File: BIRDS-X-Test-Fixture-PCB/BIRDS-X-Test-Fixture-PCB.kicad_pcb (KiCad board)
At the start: 2 copper layers, 0 parts

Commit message: Layout and label PCB
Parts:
- added C101: 100n, Capacitor_SMD:C_1206_3216Metric_Pad1.33x1.80mm_HandSolder, F.Cu at (91.7, 43.3)
- added D_3V3: LED, LED_SMD:LED_1206_3216Metric_Pad1.42x1.75mm_HandSolder, F.Cu at (117.1, 90.1)
- added D_5V0: LED, LED_SMD:LED_1206_3216Metric_Pad1.42x1.75mm_HandSolder, F.Cu at (117.1, 73.6)
- added H1: MountingHole, MountingHole:MountingHole_4mm, F.Cu at (81.5, 43.3)
- added H2: MountingHole, MountingHole:MountingHole_4mm, F.Cu at (81.5, 132.2)
- added H3: MountingHole, MountingHole:MountingHole_4mm, F.Cu at (169.2, 132.2)
- added H4: MountingHole, MountingHole:MountingHole_4mm, F.Cu at (169.2, 43.3)
- added H_3V3_1: MountingHole_Pad, MountingHole:MountingHole_4mm_Pad_Via, F.Cu at (125.6, 132.2)
- added H_3V3_2: MountingHole_Pad, MountingHole:MountingHole_4mm_Pad_Via, F.Cu at (135.7, 132.2)
- added H_5V_1: MountingHole_Pad, MountingHole:MountingHole_4mm_Pad_Via, F.Cu at (147.2, 132.2)
- added H_5V_2: MountingHole_Pad, MountingHole:MountingHole_4mm_Pad_Via, F.Cu at (156.5, 132.2)
- added H_GND_1: MountingHole_Pad, MountingHole:MountingHole_4mm_Pad_Via, F.Cu at (114.1, 132.2)
- added H_GND_2: MountingHole_Pad, MountingHole:MountingHole_4mm_Pad_Via, F.Cu at (104.4, 132.2)
- added H_GND_3: MountingHole_Pad, MountingHole:MountingHole_4mm_Pad_Via, F.Cu at (94.6, 132.2)
- added J101: LPC-50M2LG, Connector_PinHeader_2.00mm:PinHeader_2x25_P2.00mm_Horizontal, F.Cu at (81.0, 112.3)
- added J102: Conn_01x05, Connector_PinHeader_2.54mm:PinHeader_1x05_P2.54mm_Vertical, F.Cu at (148.6, 82.5)
- added J103: ~, Connector_PinHeader_2.54mm:PinHeader_2x25_P2.54mm_Vertical, F.Cu at (129.8, 119.5)
- added J104: ~, Connector_PinHeader_2.54mm:PinHeader_2x25_P2.54mm_Vertical, F.Cu at (96.8, 119.5)
- added J105: Conn_01x06, Connector_PinHeader_2.54mm:PinHeader_1x06_P2.54mm_Vertical, F.Cu at (105.7, 58.5)
- added J109: Conn_01x05, Connector_PinHeader_2.54mm:PinHeader_1x05_P2.54mm_Vertical, F.Cu at (166.6, 52.2)
- added J110: Conn_02x05_Odd_Even, Connector_IDC:IDC-Header_2x05_P2.54mm_Latch_Vertical, F.Cu at (166.6, 77.6)
- added J111: Conn_02x05_Odd_Even, Connector_IDC:IDC-Header_2x05_P2.54mm_Latch_Vertical, F.Cu at (150.1, 52.2)
- added JP101: Jumper_3_Open, Connector_PinHeader_2.54mm:PinHeader_1x03_P2.54mm_Vertical, F.Cu at (113.0, 59.7)
- added J_3V3_1: Screw_Terminal_01x02, TerminalBlock:TerminalBlock_bornier-2_P5.08mm, F.Cu at (132.3, 43.3)
- added J_3V3_2: Screw_Terminal_01x02, TerminalBlock:TerminalBlock_bornier-2_P5.08mm, F.Cu at (167.9, 109.3)
- added J_5V_1: Screw_Terminal_01x02, TerminalBlock:TerminalBlock_bornier-2_P5.08mm, F.Cu at (167.9, 120.8)
- added J_5V_2: Screw_Terminal_01x02, TerminalBlock:TerminalBlock_bornier-2_P5.08mm, F.Cu at (119.6, 43.3)
- added R_3V3: 1k, Resistor_THT:R_Axial_DIN0411_L9.9mm_D3.6mm_P12.70mm_Horizontal, F.Cu at (112.0, 83.9)
- added R_5V0: 2.2k, Resistor_THT:R_Axial_DIN0411_L9.9mm_D3.6mm_P12.70mm_Horizontal, F.Cu at (112.0, 66.2)
- added SW_3V3_EN_DIO1: SW_SPDT, Button_Switch_THT:SW_Slide_1P2T_CK_OS102011MS2Q, F.Cu at (101.7, 50.4)
- added SW_5V_EN_DIO2: SW_SPDT, Button_Switch_THT:SW_Slide_1P2T_CK_OS102011MS2Q, F.Cu at (108.2, 50.4)
- added SW_RST1: SW_Push, Button_Switch_THT:SW_PUSH_6mm, F.Cu at (88.2, 48.5)
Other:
- board outline added: 97.3 x 99.3 mm
- board text added: "3V"
- board text added: "3V3 EN"
- board text added: "5V"
- board text added: "5V EN"
- board text added: "DIO Level"
- board text added: "G"
- board text added: "RX"
- board text added: "ST_CLK"
- board text added: "ST_DIO"
- board text added: "ST_RST"
- board text added: "SW: Triangle =+V=ON"
- board text added: "TX"
- board text added: "TX,RX"

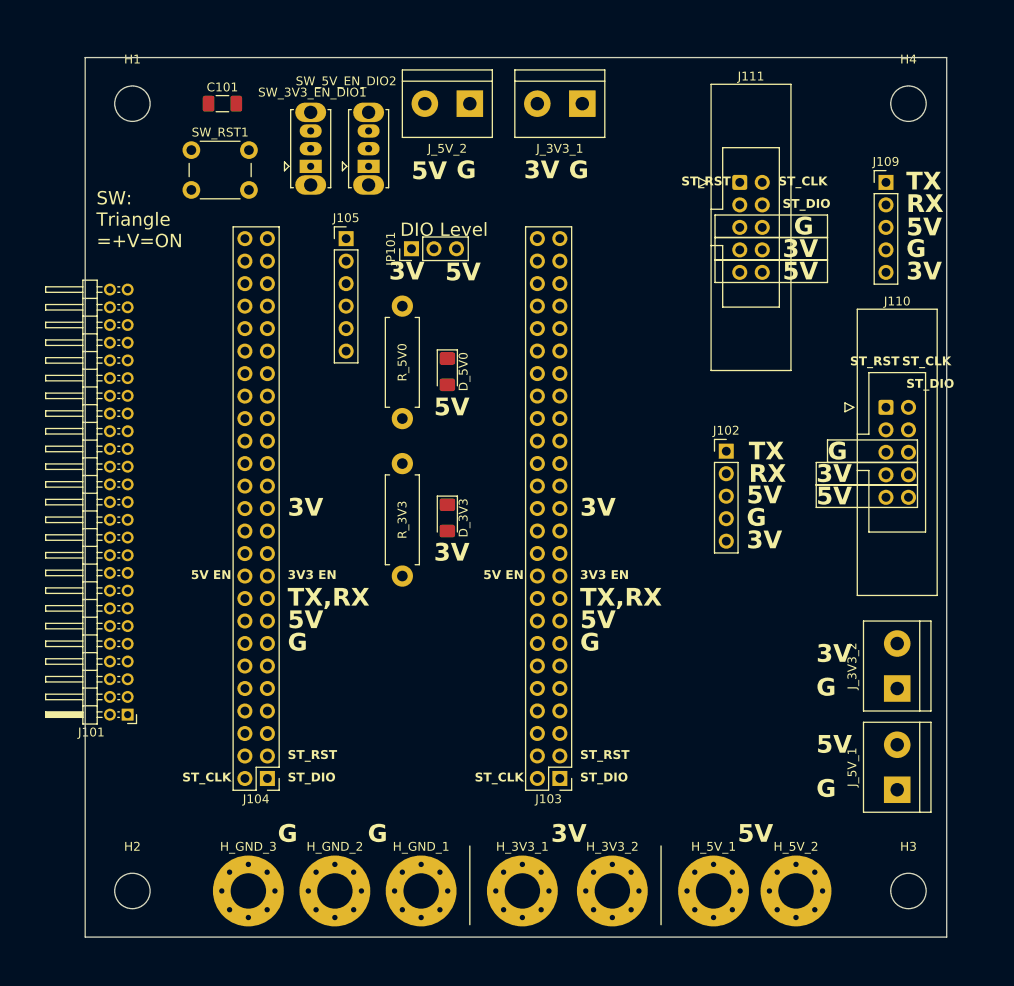
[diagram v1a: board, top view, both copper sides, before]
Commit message: Finish test fixture
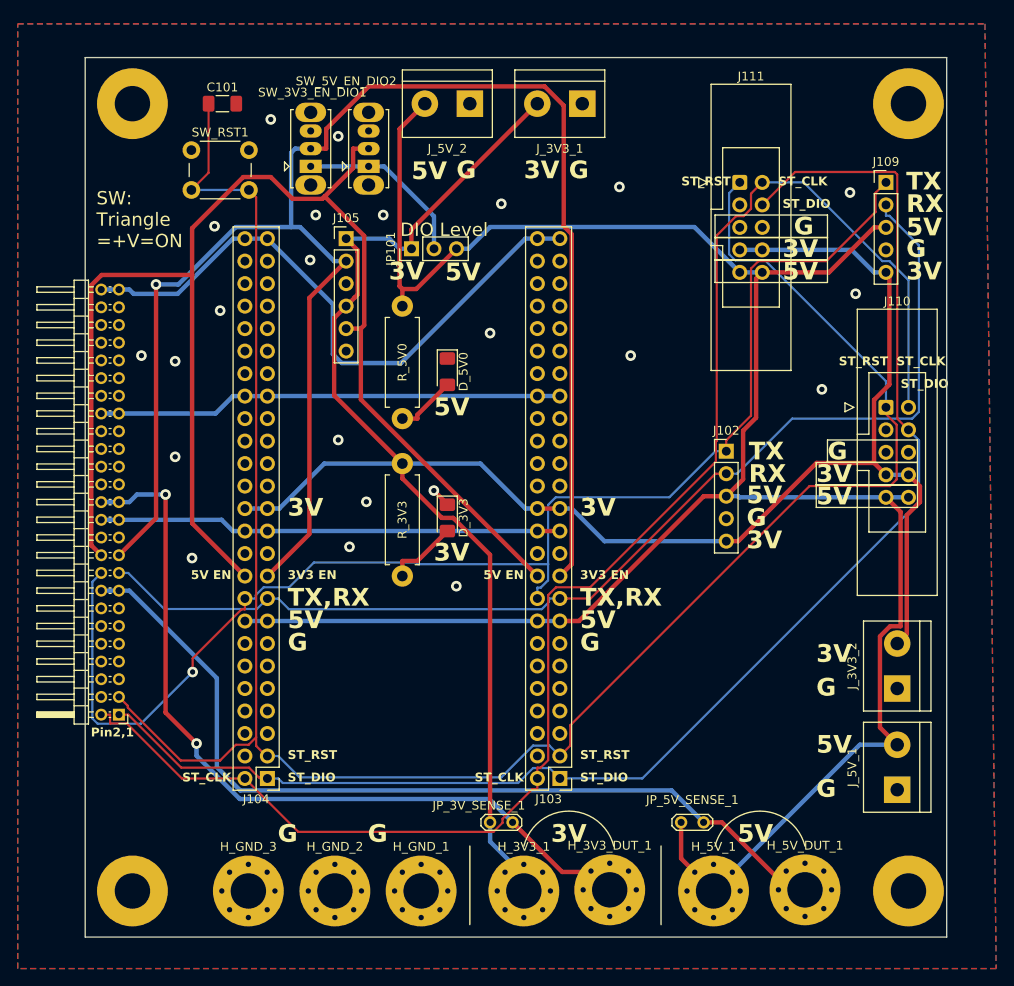
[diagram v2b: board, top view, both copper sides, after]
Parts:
- removed H_3V3_2, H_5V_2: MountingHole_Pad, MountingHole:MountingHole_4mm_Pad_Via
- added H_3V3_DUT_1: MountingHole_Pad, MountingHole:MountingHole_4mm_Pad_Via, F.Cu at (135.4, 132.1)
- added H_5V_DUT_1: MountingHole_Pad, MountingHole:MountingHole_4mm_Pad_Via, F.Cu at (157.5, 132.1)
- added JP_3V_SENSE_1: Jumper_2_Bridged, TestPoint:TestPoint_2Pads_Pitch2.54mm_Drill0.8mm, F.Cu at (124.5, 124.5)
- added JP_5V_SENSE_1: Jumper_2_Bridged, TestPoint:TestPoint_2Pads_Pitch2.54mm_Drill0.8mm, F.Cu at (146.0, 124.5)
- H1, H2, H3, H4: footprint MountingHole:MountingHole_4mm -> MountingHole:MountingHole_4mm_Pad
- moved J101 0.98 mm to (80.0, 112.3)
- moved H_3V3_1 0.16 mm to (125.7, 132.2)
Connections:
- J101 pad 15: SUP_5V0 -> /5V_DUT
- J101 pad 16: SUP_5V0 -> /5V_DUT
- J101 pad 25: SUP_3V3_2 -> /3V3_DUT
- J101 pad 26: SUP_3V3_2 -> /3V3_DUT
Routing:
- net SUP_3V3_2: track 0.00 -> 276.9 mm
- net SUP_5V0: track 0.00 -> 275.5 mm
- net ST_RST: track 0.00 -> 233.7 mm
- net DIO1_3V3_EN_FROM_BOSS: track 0.00 -> 195.8 mm, vias 0 -> 1
- net ST_SWDCLK: track 0.00 -> 175.0 mm
- net DIO2_5V_EN_FROM_BOSS: track 0.00 -> 166.3 mm
- net ST_SWDIO: track 0.00 -> 162.5 mm
- net /UART_TX_JASPER_TO_BOSS: track 0.00 -> 154.3 mm, vias 0 -> 1
- net /UART_RX_BOSS_TO_JASPER: track 0.00 -> 127.6 mm
- net /5V_DUT: track 0.00 -> 115.7 mm
- net /3V3_DUT: track 0.00 -> 108.0 mm, vias 0 -> 2
- net SUP_3V3_1: track 0.00 -> 69.5 mm
- net SUP_UNREG_2: track 0.00 -> 52.6 mm
- net SUP_UNREG_1: track 0.00 -> 52.3 mm
- net Net-(JP101-C): track 0.00 -> 19.9 mm
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- added copper zone on B.Cu, net GND
- added copper zone on F.Cu, net GND
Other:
- board text added: "Pin2,1"

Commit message: Update labels on test fixture
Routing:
- net SUP_5V0: track 275.5 -> 276.6 mm
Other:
- board text added: "JASPER BIRDS-X Test Fixture Rev1, 2023-08-22 AlbertaSat x CalgaryToSpace"
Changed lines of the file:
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@@
     (property "ki_keywords" "Jumper SPST")
     (attr exclude_from_pos_files)
-    (fp_text reference "JP_5V_SENSE_1" (at 1.27 2.54) (layer "F.SilkS")
+    (fp_text reference "JP_5V_SENSE_1" (at 1.25 2.54) (layer "F.SilkS")
         (effects (font (size 1 1) (thickness 0.15)))
     )
@@
       (net 113 "/5V_DUT") (pinfunction "1") (pintype "input"))
   )
+  (gr_rect (start 106.045 121.6025) (end 120.015 99.3775)
+    (stroke (width 0.15) (type solid)) (fill solid) (layer "B.SilkS"))
+  (gr_rect (start 87.63 95.25) (end 105.41 97.79)
+    (stroke (width 0.15) (type default)) (fill none) (layer "F.SilkS"))
+  (gr_rect (start 90.805 102.87) (end 102.87 105.41)
+    (stroke (width 0.15) (type default)) (fill none) (layer "F.SilkS"))
   (gr_rect (start 147.32 55.88) (end 160.02 58.42)
+    (stroke (width 0.15) (type default)) (fill none) (layer "F.SilkS"))
+  (gr_rect (start 92.075 86.995) (end 103.505 90.17)
     (stroke (width 0.15) (type default)) (fill none) (layer "F.SilkS"))
   (gr_rect (start 160.02 81.28) (end 170.18 83.82)
     (stroke (width 0.15) (type default)) (fill none) (layer "F.SilkS"))
-  (gr_rect (start 160.02 63.5) (end 147.32 60.96)
+  (gr_rect (start 147.32 60.96) (end 160.02 63.5)
     (stroke (width 0.15) (type default)) (fill none) (layer "F.SilkS"))
   (gr_arc (start 125.73 127.156344) (mid 130.81 123.19) (end 135.89 127.156344)
     (stroke (width 0.15) (type default)) (layer "F.SilkS"))
-  (gr_rect (start 170.18 88.9) (end 158.75 86.36)
+  (gr_rect (start 120.65 95.25) (end 138.43 97.79)
     (stroke (width 0.15) (type default)) (fill none) (layer "F.SilkS"))
-  (gr_rect (start 160.02 60.96) (end 147.32 58.42)
+  (gr_rect (start 141.605 97.79) (end 155.575 120.015)
+    (stroke (width 0.15) (type solid)) (fill solid) (layer "F.SilkS"))
+  (gr_rect (start 125.095 102.87) (end 135.255 105.41)
+    (stroke (width 0.15) (type default)) (fill none) (layer "F.SilkS"))
+  (gr_rect (start 124.46 87.63) (end 137.16 90.17)
+    (stroke (width 0.15) (type default)) (fill none) (layer "F.SilkS"))
+  (gr_rect (start 158.75 86.36) (end 170.18 88.9)
+    (stroke (width 0.15) (type default)) (fill none) (layer "F.SilkS"))
+  (gr_rect (start 105.41 101.6) (end 120.015 120.9675)
+    (stroke (width 0.15) (type solid)) (fill solid) (layer "F.SilkS"))
+  (gr_rect (start 147.32 58.42) (end 160.02 60.96)
     (stroke (width 0.15) (type default)) (fill none) (layer "F.SilkS"))
   (gr_line (start 141.224 127.127) (end 141.224 136.017)
@@
   (gr_rect (start 76.2 38.1) (end 173.482 137.414)
     (stroke (width 0.1) (type default)) (fill none) (layer "Edge.Cuts"))
+  (gr_text "JASPER BIRDS-X Test Fixture\nRev1, 2023-08-22\nAlbertaSat x CalgaryToSpace" (at 139.7 90.805 -90) (layer "B.SilkS")
+    (effects (font (size 2 2) (thickness 0.4) bold) (justify mirror))
+  )
   (gr_text "3V" (at 99.06 88.9) (layer "F.SilkS")
     (effects (font (size 2 2) (thickness 0.4) bold) (justify left))
@@
     (effects (font (size 1 1) (thickness 0.2) bold) (justify right))
   )
-  (gr_text "ST_RST" (at 161.29 72.39) (layer "F.SilkS")
+  (gr_text "ST_RST" (at 160.02 76.2) (layer "F.SilkS")
     (effects (font (size 1 1) (thickness 0.2) bold) (justify left))
   )
@@
   (gr_text "G" (at 150.876 90.043) (layer "F.SilkS")
     (effects (font (size 2 2) (thickness 0.4) bold) (justify left))
+  )
+  (gr_text "JASPER BIRDS-X Test Fixture\nRev1, 2023-08-22\nAlbertaSat x CalgaryToSpace" (at 139.065 62.865 90) (layer "F.SilkS")
+    (effects (font (size 2 2) (thickness 0.4) bold))
   )
   (gr_text "SW:\nTriangle\n=+V=ON" (at 77.47 59.69) (layer "F.SilkS")
@@
   (segment (start 96.774 89.027) (end 98.124 89.027) (width 0.5) (layer "B.Cu") (net 3))
   (segment (start 129.799 89.022) (end 131.149 89.022) (width 0.5) (layer "B.Cu") (net 3))
+  (segment (start 163.83 102.87) (end 168.275 98.425) (width 0.5) (layer "F.Cu") (net 4))
+  (segment (start 167.894 115.697) (end 163.83 111.633) (width 0.5) (layer "F.Cu") (net 4))
   (segment (start 150.495 85.725) (end 148.59 87.63) (width 0.5) (layer "F.Cu") (net 4))
   (segment (start 131.958 101.722) (end 146.05 87.63) (width 0.5) (layer "F.Cu") (net 4))
-  (segment (start 168.275 89.408) (end 166.624 87.757) (width 0.5) (layer "F.Cu") (net 4))
   (segment (start 112.014 64.2356) (end 112.014 66.167) (width 0.5) (layer "F.Cu") (net 4))
   (segment (start 149.2766 130.0857) (end 150.1553 130.9644) (width 0.5) (layer "F.Cu") (net 4))
@@
   (segment (start 145.9127 132.207) (end 145.034 133.0857) (width 0.5) (layer "F.Cu") (net 4))
   (segment (start 147.1553 132.207) (end 145.9127 132.207) (width 0.5) (layer "F.Cu") (net 4))
-  (segment (start 165.944 113.747) (end 165.944 103.459283) (width 0.5) (layer "F.Cu") (net 4))
   (segment (start 151.959 78.769172) (end 150.495 80.233172) (width 0.5) (layer "F.Cu") (net 4))
   (segment (start 113.5794 64.2356) (end 112.014 64.2356) (width 0.5) (layer "F.Cu") (net 4))
@@
   (segment (start 143.49 128.5417) (end 143.49 124.46) (width 0.5) (layer "F.Cu") (net 4))
   (segment (start 150.495 80.233172) (end 150.495 85.725) (width 0.5) (layer "F.Cu") (net 4))
-  (segment (start 167.894 115.697) (end 165.944 113.747) (width 0.5) (layer "F.Cu") (net 4))
+  (segment (start 168.275 98.425) (end 168.275 89.408) (width 0.5) (layer "F.Cu") (net 4))
   (segment (start 150.1553 133.4496) (end 150.1553 132.207) (width 0.5) (layer "F.Cu") (net 4))
   (segment (start 111.7006 63.9222) (end 111.7006 46.1604) (width 0.5) (layer "F.Cu") (net 4))
-  (segment (start 165.944 103.459283) (end 167.086283 102.317) (width 0.5) (layer "F.Cu") (net 4))
+  (segment (start 168.275 89.408) (end 166.624 87.757) (width 0.5) (layer "F.Cu") (net 4))
+  (segment (start 163.83 111.633) (end 163.83 102.87) (width 0.5) (layer "F.Cu") (net 4))
   (segment (start 112.014 64.2356) (end 111.7006 63.9222) (width 0.5) (layer "F.Cu") (net 4))
   (segment (start 146.05 87.63) (end 148.59 87.63) (width 0.5) (layer "F.Cu") (net 4))
   (segment (start 160.194 62.357) (end 165.274 57.277) (width 0.5) (layer "F.Cu") (net 4))
-  (segment (start 168.275 102.317) (end 168.275 89.408) (width 0.5) (layer "F.Cu") (net 4))
   (segment (start 111.7006 46.1604) (end 114.554 43.307) (width 0.5) (layer "F.Cu") (net 4))
   (segment (start 144.1553 130.9644) (end 144.1553 132.207) (width 0.5) (layer "F.Cu") (net 4))
   (segment (start 145.034 130.0857) (end 144.1553 130.9644) (width 0.5) (layer "F.Cu") (net 4))
-  (segment (start 167.086283 102.317) (end 168.275 102.317) (width 0.5) (layer "F.Cu") (net 4))
   (segment (start 151.959 63.052) (end 151.959 78.769172) (width 0.5) (layer "F.Cu") (net 4))
   (segment (start 145.034 133.0857) (end 145.034 134.3283) (width 0.5) (layer "F.Cu") (net 4))
